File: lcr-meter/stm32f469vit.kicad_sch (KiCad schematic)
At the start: 1 part, among them U22 STM32F469VITx

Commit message: Schematic completion
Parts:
- removed U22: STM32F469VITx, Package_QFP:LQFP-100_14x14mm_P0.5mm, symbol MCU_ST_STM32F4:STM32F469VITx
- added C2: 100n, symbol Device:C_Small
- added C3: 2.2u, symbol Device:C_Small
- added C4, C5: 4.3pF, symbol Device:C_Small
- added C6, C7: 1u, symbol Device:C_Small
- added J1: Conn_ARM_SWD_TagConnect_TC2030-NL, Connector:Tag-Connect_TC2030-IDC-NL_2x03_P1.27mm_Vertical, symbol Connector:Conn_ARM_SWD_TagConnect_TC2030-NL
- added R1, R10, R5: 10k, symbol Device:R_Small
- added R4, R8: 1k, symbol Device:R_Small
- added SW1, SW2: SW_MEC_5E, symbol Switch:SW_MEC_5E
- added U5: STM32F446RETx, Package_QFP:LQFP-64_10x10mm_P0.5mm, symbol MCU_ST_STM32F4:STM32F446RETx
- added Y1: 8 MHz, symbol Device:Crystal_Small
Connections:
- new net: C7.1, R10.1, R8.2
- new net: C3.1, U5.30 (VCAP_1)
- new net: R1.1, U5.60 (BOOT0)
- new net: C6.1, R4.2, R5.1
- new net +3V3: J1.1 (VCC), R10.2, R5.2, U5.1 (VBAT), U5.13 (VDDA), U5.19 (VDD), U5.32 (VDD), U5.48 (VDD), U5.64 (VDD)
- new net AD9833_NCS: U5.41 (PA8)
- new net Button 0: R4.1, SW1.3 (K), SW1.4 (A), U5.35 (PB14)
- new net Button 1: R8.1, SW2.3 (K), SW2.4 (A), U5.36 (PB15)
- new net GND: C2.2, C3.2, C4.2, C5.2, C6.2, C7.2, J1.5 (GND), R1.2, SW1.1, SW1.2, SW2.1, SW2.2, U5.12 (VSSA), U5.18 (VSS), U5.31 (VSS), U5.47 (VSS), U5.63 (VSS)
- new net LCD_DC: U5.10 (PC2)
- new net LCD_LED: U5.11 (PC3)
- new net LCD_NCS: U5.8 (PC0)
- new net LCD_RST: U5.9 (PC1)
- new net MCP3202_NCS: U5.42 (PA9)
- new net OSC_IN: C4.1, U5.5 (PH0), Y1.2
- new net OSC_OUT: C5.1, U5.6 (PH1), Y1.1
- new net RESET\: C2.1, J1.3 (~{RESET}), U5.7 (NRST)
- new net SPI1_MISO: U5.22 (PA6)
- new net SPI1_MOSI: U5.23 (PA7)
- new net SPI1_SCK: U5.21 (PA5)
- new net SPI3_MISO: U5.52 (PC11)
- new net SPI3_MOSI: U5.28 (PB2)
- new net SPI3_SCK: U5.51 (PC10)
- new net STM32_ADC1_IN0: U5.14 (PA0)
- new net STM32_ADC2_IN1: U5.15 (PA1)
- new net SWCLK: J1.4 (SWCLK), U5.49 (PA14)
- new net SWDIO: J1.2 (SWDIO), U5.46 (PA13)
- new net SWO: J1.6 (SWO), U5.55 (PB3)
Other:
- note added: "HF Oscillator"
- note added: "SWD"
- note added: "User Buttons"

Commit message: Schematic polishing
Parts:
- added C12, C15, C16, C17, C19, C20, C21: 100n, Capacitor_SMD:C_0402_1005Metric, symbol Device:C_Small
- added C13: 1u, Capacitor_SMD:C_0402_1005Metric, symbol Device:C_Small
- added C14: 4.7u, Capacitor_SMD:C_0402_1005Metric, symbol Device:C_Small
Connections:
- net +3V3: now also C12.1, C13.1, C14.1, C15.1, C16.1, C17.1, C19.1, C20.1, C21.1
- net GND: now also C12.2, C13.2, C14.2, C15.2, C16.2, C17.2, C19.2, C20.2, C21.2
- net Range_0: now reaches U5.57 (PB5)
- net Range_1: now reaches U5.58 (PB6)
- net Range_2: now reaches U5.59 (PB7)
- net Range_3: now reaches U5.61 (PB8)
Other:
- note added: "Extra VDDA decoupling"
- note added: "Supply Decoupling"
- note added: "Time Constant = RC = 1 ms Should be more than enough to remove debouncing"
- moved on the sheet: C2, C3, C4, C5, C6, C7, R1, R10, R4, R5, R8, SW1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

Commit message: Schematic polishing
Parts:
- C14: footprint Capacitor_SMD:C_0402_1005Metric -> Capacitor_SMD:C_0805_2012Metric
- C2, C3, C4, C5, C6, C7: footprint (none) -> Capacitor_SMD:C_0402_1005Metric
- R1, R10, R4, R5, R8: footprint (none) -> Resistor_SMD:R_0402_1005Metric
- SW1, SW2: footprint (none) -> Button_Switch_THT:SW_PUSH_6mm_H5mm
- Y1: footprint (none) -> footprints:XTAL_CG04874_NDK-L
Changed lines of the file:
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@@
 			)
 		)
-		(property "Footprint" ""
+		(property "Footprint" "Capacitor_SMD:C_0402_1005Metric"
 			(at 63.5 127 0)
 			(effects
@@
 			)
 		)
-		(property "Footprint" ""
+		(property "Footprint" "Button_Switch_THT:SW_PUSH_6mm_H5mm"
 			(at 39.37 129.54 0)
 			(effects
@@
 			)
 		)
-		(property "Footprint" ""
+		(property "Footprint" "Capacitor_SMD:C_0402_1005Metric"
 			(at 120.65 46.99 0)
 			(effects
@@
 			)
 		)
-		(property "Footprint" ""
+		(property "Footprint" "footprints:XTAL_CG04874_NDK-L"
 			(at 113.03 41.91 0)
 			(effects
@@
 			)
 		)
-		(property "Footprint" ""
+		(property "Footprint" "Capacitor_SMD:C_0402_1005Metric"
 			(at 171.45 52.07 0)
 			(effects
@@
 			)
 		)
-		(property "Footprint" ""
+		(property "Footprint" "Capacitor_SMD:C_0402_1005Metric"
 			(at 105.41 46.99 0)
 			(effects
@@
 			)
 		)
-		(property "Footprint" ""
+		(property "Footprint" "Capacitor_SMD:C_0402_1005Metric"
 			(at 63.5 91.44 0)
 			(effects
@@
 			)
 		)
-		(property "Footprint" ""
+		(property "Footprint" "Resistor_SMD:R_0402_1005Metric"
 			(at 182.88 57.15 0)
 			(effects
@@
 			)
 		)
-		(property "Footprint" ""
+		(property "Footprint" "Resistor_SMD:R_0402_1005Metric"
 			(at 55.88 124.46 0)
 			(effects
@@
 			)
 		)
-		(property "Footprint" "Capacitor_SMD:C_0402_1005Metric"
+		(property "Footprint" "Capacitor_SMD:C_0805_2012Metric"
 			(at 118.11 83.82 0)
 			(effects
@@
 			)
 		)
-		(property "Footprint" ""
+		(property "Footprint" "Resistor_SMD:R_0402_1005Metric"
 			(at 63.5 83.82 0)
 			(effects
@@
 			)
 		)
-		(property "Footprint" ""
+		(property "Footprint" "Button_Switch_THT:SW_PUSH_6mm_H5mm"
 			(at 39.37 93.98 0)
 			(effects
@@
 			)
 		)
-		(property "Footprint" ""
+		(property "Footprint" "Capacitor_SMD:C_0402_1005Metric"
 			(at 191.77 118.11 0)
 			(effects
@@
 			)
 		)
-		(property "Footprint" ""
+		(property "Footprint" "Resistor_SMD:R_0402_1005Metric"
 			(at 55.88 88.9 0)
 			(effects
@@
 			)
 		)
-		(property "Footprint" ""
+		(property "Footprint" "Resistor_SMD:R_0402_1005Metric"
 			(at 63.5 119.38 0)
 			(effects

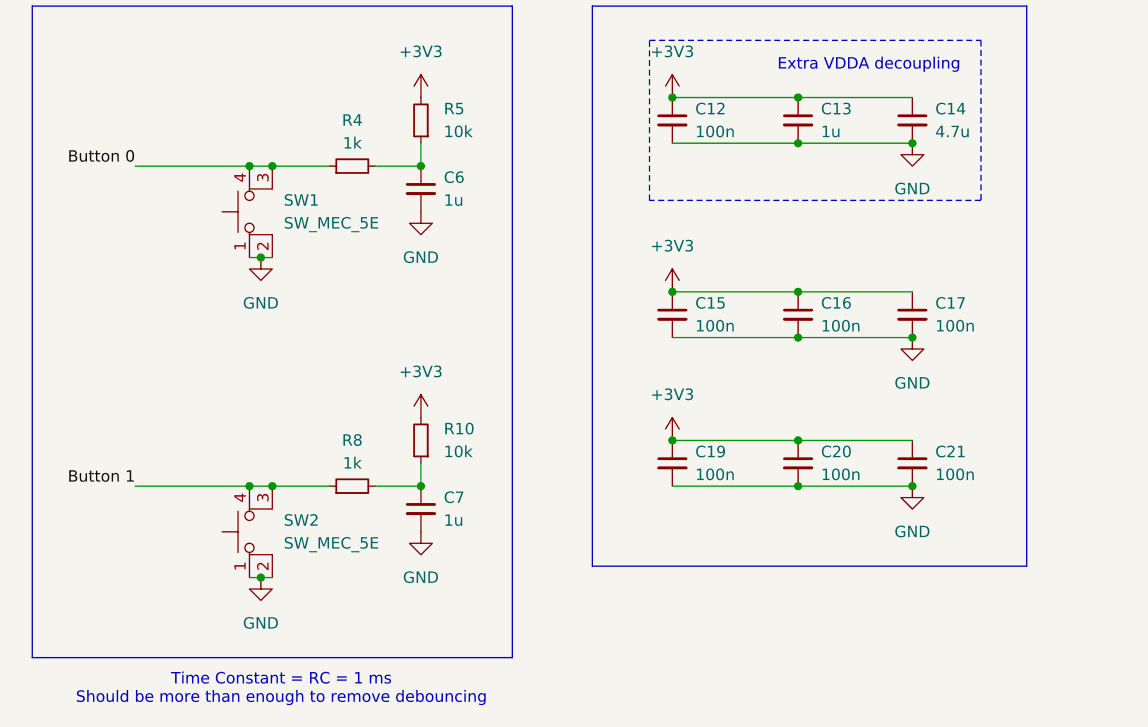
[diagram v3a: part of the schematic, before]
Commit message: Component grouping started
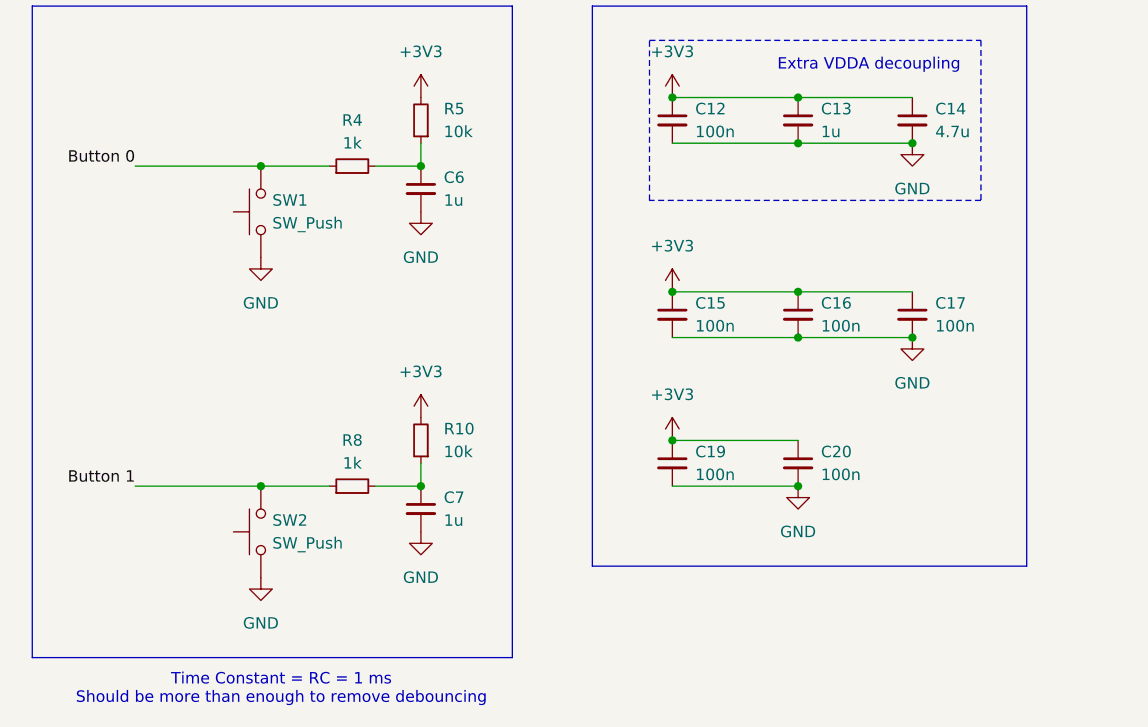
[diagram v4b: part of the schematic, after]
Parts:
- removed C21: 100n, Capacitor_SMD:C_0402_1005Metric, symbol Device:C_Small
- removed SW1, SW2: SW_MEC_5E, Button_Switch_THT:SW_PUSH_6mm_H5mm, symbol Switch:SW_MEC_5E
- added SW1, SW2: SW_Push, Button_Switch_THT:SW_PUSH_6mm_H5mm, symbol Switch:SW_Push
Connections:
- net Button 0: now also SW1.2
- net Button 1: now also SW2.2
- net GND: now also SW1.1, SW2.1

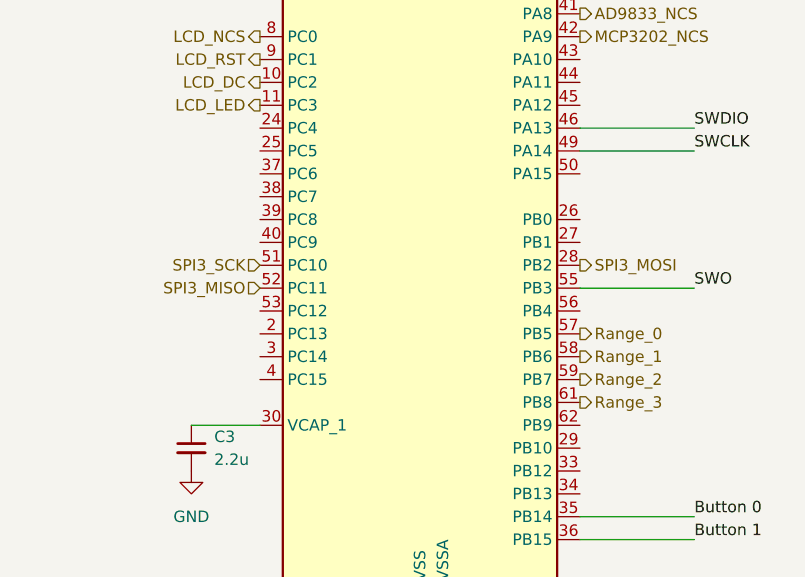
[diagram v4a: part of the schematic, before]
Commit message: Order submitteed, Mod board submitted
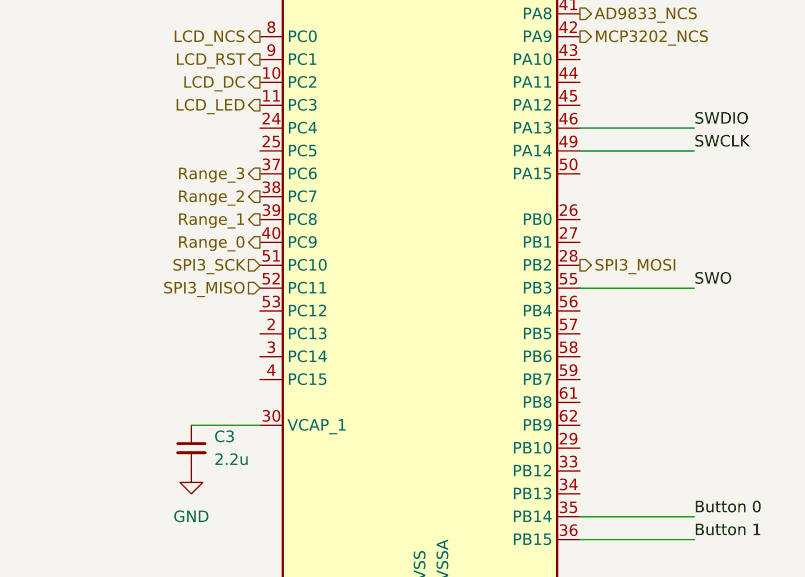
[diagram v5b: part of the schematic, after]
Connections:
- net Range_0: now also U5.40 (PC9); no longer U5.57 (PB5)
- net Range_1: now also U5.39 (PC8); no longer U5.58 (PB6)
- net Range_2: now also U5.38 (PC7); no longer U5.59 (PB7)
- net Range_3: now also U5.37 (PC6); no longer U5.61 (PB8)
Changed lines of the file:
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@@
 	(hierarchical_label "Range_3"
 		(shape output)
-		(at 234.95 113.03 0)
+		(at 199.39 87.63 180)
 		(fields_autoplaced yes)
 		(effects
@@
 				(size 1.27 1.27)
 			)
-			(justify left)
+			(justify right)
 		)
 	)
@@
 	(hierarchical_label "Range_2"
 		(shape output)
-		(at 234.95 110.49 0)
+		(at 199.39 90.17 180)
 		(fields_autoplaced yes)
 		(effects
@@
 				(size 1.27 1.27)
 			)
-			(justify left)
+			(justify right)
 		)
 	)
@@
 	(hierarchical_label "Range_0"
 		(shape output)
-		(at 234.95 105.41 0)
+		(at 199.39 95.25 180)
 		(fields_autoplaced yes)
 		(effects
@@
 				(size 1.27 1.27)
 			)
-			(justify left)
+			(justify right)
 		)
 	)
@@
 	(hierarchical_label "Range_1"
 		(shape output)
-		(at 234.95 107.95 0)
+		(at 199.39 92.71 180)
 		(fields_autoplaced yes)
 		(effects
@@
 				(size 1.27 1.27)
 			)
-			(justify left)
+			(justify right)
 		)
 	)

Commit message: Rev A schematic fixes
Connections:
- net Button 0: now also C6.1, R4.2, R5.1; no longer R4.1, SW1.2
- net Button 1: now also C7.1, R10.1, R8.2; no longer R8.1, SW2.2
- new net: R4.1, SW1.2
- new net: R8.1, SW2.2
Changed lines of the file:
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@@
 	(paper "A4")
 	(junction
+		(at 60.96 124.46)
+		(diameter 0)
+		(color 0 0 0 0)
+	)
+	(junction
 		(at 105.41 107.95)
 		(diameter 0)
@@
 	)
 	(junction
-		(at 45.72 88.9)
-		(diameter 0)
-		(color 0 0 0 0)
-	)
-	(junction
 		(at 63.5 124.46)
 		(diameter 0)
@@
 	)
 	(junction
+		(at 60.96 88.9)
+		(diameter 0)
+		(color 0 0 0 0)
+	)
+	(junction
 		(at 118.11 107.95)
 		(diameter 0)
@@
 		(color 0 0 0 0)
 	)
-	(junction
-		(at 45.72 124.46)
-		(diameter 0)
-		(color 0 0 0 0)
-	)
 	(wire
 		(pts
@@
 	(wire
 		(pts
-			(xy 58.42 124.46) (xy 63.5 124.46)
+			(xy 58.42 124.46) (xy 60.96 124.46)
 		)
 		(stroke
@@
 	(wire
 		(pts
+			(xy 60.96 81.28) (xy 60.96 88.9)
+		)
+		(stroke
+			(width 0)
+			(type default)
+		)
+	)
+	(wire
+		(pts
 			(xy 212.09 44.45) (xy 214.63 44.45)
 		)
@@
 	(wire
 		(pts
-			(xy 31.75 88.9) (xy 45.72 88.9)
+			(xy 31.75 81.28) (xy 60.96 81.28)
 		)
 		(stroke
@@
 	(wire
 		(pts
-			(xy 31.75 124.46) (xy 45.72 124.46)
-		)
-		(stroke
-			(width 0)
-			(type default)
-		)
-	)
-	(wire
-		(pts
 			(xy 105.41 81.28) (xy 118.11 81.28)
 		)
@@
 	(wire
 		(pts
+			(xy 60.96 88.9) (xy 63.5 88.9)
+		)
+		(stroke
+			(width 0)
+			(type default)
+		)
+	)
+	(wire
+		(pts
 			(xy 105.41 102.87) (xy 118.11 102.87)
 		)
@@
 	(wire
 		(pts
+			(xy 31.75 116.84) (xy 60.96 116.84)
+		)
+		(stroke
+			(width 0)
+			(type default)
+		)
+	)
+	(wire
+		(pts
+			(xy 60.96 116.84) (xy 60.96 124.46)
+		)
+		(stroke
+			(width 0)
+			(type default)
+		)
+	)
+	(wire
+		(pts
 			(xy 91.44 119.38) (xy 105.41 119.38)
 		)
@@
 	(wire
 		(pts
-			(xy 58.42 88.9) (xy 63.5 88.9)
+			(xy 58.42 88.9) (xy 60.96 88.9)
+		)
+		(stroke
+			(width 0)
+			(type default)
+		)
+	)
+	(wire
+		(pts
+			(xy 60.96 124.46) (xy 63.5 124.46)
 		)
 		(stroke
@@
 	)
 	(label "Button 1"
-		(at 31.75 124.46 180)
+		(at 31.75 116.84 180)
 		(fields_autoplaced yes)
 		(effects
@@
 	)
 	(label "Button 0"
-		(at 31.75 88.9 180)
-		(fields_autoplaced yes)
-		(effects
+		(at 31.75 81.28 180)
+		(fields_autoplaced yes)
+		(effects

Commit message: REV B order submitted
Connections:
- net MCP3202_NCS: no longer names the net of U5.42 (PA9)
- no-connect marks 0 -> 1
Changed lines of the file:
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@@
 		(color 0 0 0 0)
+	)
+	(no_connect
+		(at 234.95 72.39)
 	)
 	(wire
@@
 		)
 	)
-	(hierarchical_label "MCP3202_NCS"
-		(shape output)
-		(at 234.95 72.39 0)
-		(fields_autoplaced yes)
-		(effects
-			(font
-				(size 1.27 1.27)
-			)
-			(justify left)
-		)
-	)
